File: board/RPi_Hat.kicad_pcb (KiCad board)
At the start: 2 copper layers, 65 x 56.5 mm, 33 parts, among them IC1 ATMEGA328P-P, IC2 RFM69HW, J1 RPi_GPIO, P6 SW_CONN, P7 CONN_01X01, Q1 BSS138_GSD, SW1 SWITCH, Y1 16MHz

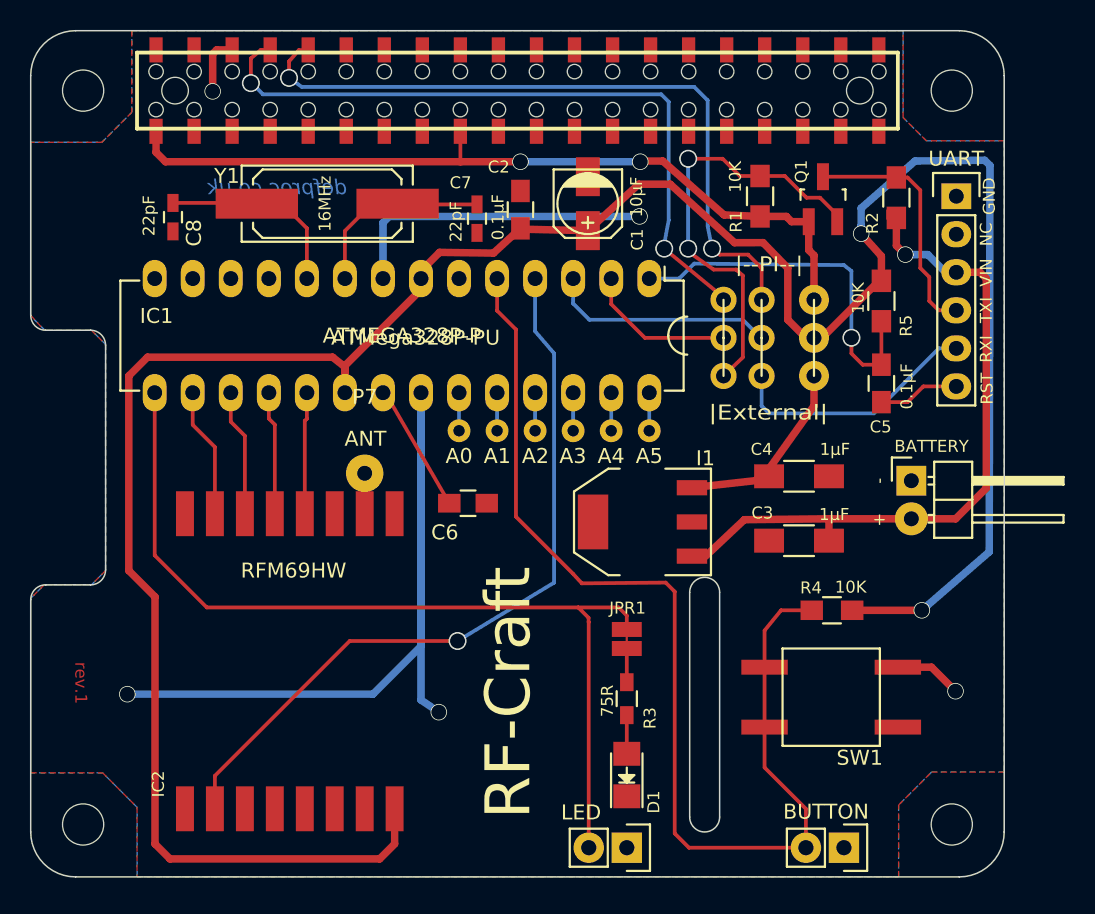
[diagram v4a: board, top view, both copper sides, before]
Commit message: revised via sizes, as per board house recommendations
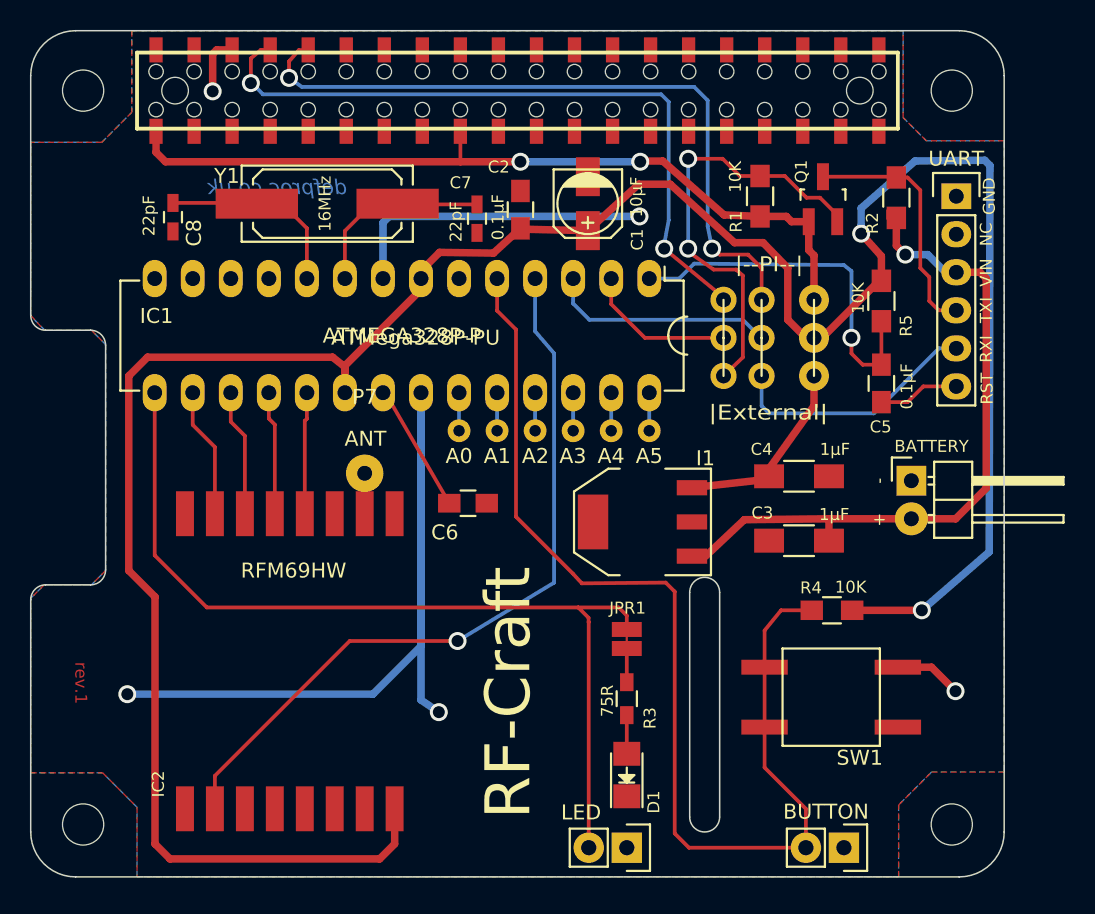
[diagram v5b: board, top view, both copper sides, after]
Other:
- net class BUS: via_dia 1.1 -> 1.2; via_drill 1 -> 0.8
- net class Default: via_drill 1 -> 0.8
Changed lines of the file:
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@@
     (edge_width 0.1)
     (via_size 1.2)
-    (via_drill 1)
+    (via_drill 0.8)
     (via_min_size 0.4)
     (via_min_drill 0.3)
@@
     (trace_width 0.25)
     (via_dia 1.2)
-    (via_drill 1)
+    (via_drill 0.8)
     (uvia_dia 0.6)
     (uvia_drill 0.4)
@@
     (clearance 0.2)
     (trace_width 0.5)
-    (via_dia 1.1)
-    (via_drill 1)
+    (via_dia 1.2)
+    (via_drill 0.8)
     (uvia_dia 0.6)
     (uvia_drill 0.4)
@@
   (gr_line (start 79.2 44.45) (end 138.2 44.45) (angle 90) (layer Edge.Cuts) (width 0.1))
   (segment (start 140.25 53.45) (end 139.9 53.1) (width 0.5) (layer B.Cu) (net 29))
-  (via (at 135.7 83.15) (size 1.1) (drill 1) (layers F.Cu B.Cu) (net 29))
+  (via (at 135.7 83.15) (size 1.2) (drill 0.8) (layers F.Cu B.Cu) (net 29))
   (segment (start 135.7 83.15) (end 140.2 79.25) (width 0.5) (layer B.Cu) (net 29))
   (segment (start 140.2 79.25) (end 140.25 53.45) (width 0.5) (layer B.Cu) (net 29))
@@
   (segment (start 133 59.5) (end 133 61.15) (width 0.5) (layer F.Cu) (net 29))
   (segment (start 131.65 58) (end 133 59.5) (width 0.5) (layer F.Cu) (net 29))
-  (via (at 131.65 58) (size 1.1) (drill 1) (layers F.Cu B.Cu) (net 29))
+  (via (at 131.65 58) (size 1.2) (drill 0.8) (layers F.Cu B.Cu) (net 29))
   (segment (start 131.65 57.45) (end 131.65 58) (width 0.5) (layer B.Cu) (net 29))
   (segment (start 135.25 53.15) (end 131.65 56.3) (width 0.5) (layer B.Cu) (net 29))
@@
   (segment (start 97.18 66.82) (end 97.18 68.62) (width 0.5) (layer F.Cu) (net 29))
   (segment (start 89.65 45.7322) (end 88.6178 45.7322) (width 0.5) (layer F.Cu) (net 30))
-  (via (at 88.35 48.5) (size 1.1) (drill 1) (layers F.Cu B.Cu) (net 30))
+  (via (at 88.35 48.5) (size 1.2) (drill 0.8) (layers F.Cu B.Cu) (net 30))
   (segment (start 88.35 46) (end 88.35 48.5) (width 0.5) (layer F.Cu) (net 30))
   (segment (start 88.6178 45.7322) (end 88.35 46) (width 0.5) (layer F.Cu) (net 30))
   (segment (start 134.1 86.95) (end 136.35 86.95) (width 0.5) (layer F.Cu) (net 30))
-  (via (at 137.95 88.55) (size 1.1) (drill 1) (layers F.Cu B.Cu) (net 30))
+  (via (at 137.95 88.55) (size 1.2) (drill 0.8) (layers F.Cu B.Cu) (net 30))
   (segment (start 136.35 86.95) (end 137.95 88.55) (width 0.5) (layer F.Cu) (net 30))
   (segment (start 99.72 61) (end 99.72 57.27) (width 0.5) (layer B.Cu) (net 30))
-  (via (at 116.85 56.85) (size 1.1) (drill 1) (layers F.Cu B.Cu) (net 30))
+  (via (at 116.85 56.85) (size 1.2) (drill 0.8) (layers F.Cu B.Cu) (net 30))
   (segment (start 100.14 56.85) (end 116.85 56.85) (width 0.5) (layer B.Cu) (net 30))
   (segment (start 99.72 57.27) (end 100.14 56.85) (width 0.5) (layer B.Cu) (net 30))
   (segment (start 102.26 68.62) (end 102.26 85.54) (width 0.5) (layer B.Cu) (net 30))
-  (via (at 82.65 88.75) (size 1.1) (drill 1) (layers F.Cu B.Cu) (net 30))
+  (via (at 82.65 88.75) (size 1.2) (drill 0.8) (layers F.Cu B.Cu) (net 30))
   (segment (start 99.05 88.75) (end 82.65 88.75) (width 0.5) (layer B.Cu) (net 30))
   (segment (start 102.26 85.54) (end 99.05 88.75) (width 0.5) (layer B.Cu) (net 30))
   (segment (start 102.26 68.62) (end 102.26 89.14) (width 0.5) (layer B.Cu) (net 30))
   (segment (start 102.26 89.14) (end 103.45 89.95) (width 0.5) (layer B.Cu) (net 30))
-  (via (at 103.45 89.95) (size 1.1) (drill 1) (layers F.Cu B.Cu) (net 30))
+  (via (at 103.45 89.95) (size 1.2) (drill 0.8) (layers F.Cu B.Cu) (net 30))
   (segment (start 138 60.58) (end 139.58 60.58) (width 0.5) (layer F.Cu) (net 31) (status 10))
   (segment (start 137.96 77.04) (end 135 77.04) (width 0.5) (layer F.Cu) (net 31))
@@
   (segment (start 137.28 60.58) (end 136.1 59.4) (width 0.5) (layer B.Cu) (net 31) (status 10))
   (segment (start 136.1 59.4) (end 134.6 59.4) (width 0.5) (layer B.Cu) (net 31))
-  (via (at 134.6 59.4) (size 1.1) (drill 1) (layers F.Cu B.Cu) (net 31))
+  (via (at 134.6 59.4) (size 1.2) (drill 0.8) (layers F.Cu B.Cu) (net 31))
   (segment (start 134.6 59.4) (end 134 58.8) (width 0.5) (layer F.Cu) (net 31))
   (segment (start 134 58.8) (end 134 56.95) (width 0.5) (layer F.Cu) (net 31))
@@
   (segment (start 117.5 61) (end 119.5 61) (width 0.25) (layer B.Cu) (net 34))
   (segment (start 131 64.95) (end 131 64.95) (width 0.25) (layer F.Cu) (net 34))
-  (via (at 131 64.95) (size 1.2) (drill 1) (layers F.Cu B.Cu) (net 34))
+  (via (at 131 64.95) (size 1.2) (drill 0.8) (layers F.Cu B.Cu) (net 34))
   (segment (start 130.5 60.1) (end 131 60.5) (width 0.25) (layer B.Cu) (net 34))
   (segment (start 131 60.5) (end 131 64.95) (width 0.25) (layer B.Cu) (net 34))
@@
   (segment (start 111.15 81.3) (end 111.15 66) (width 0.25) (layer B.Cu) (net 41))
   (segment (start 104.7 85.2) (end 111.15 81.3) (width 0.25) (layer B.Cu) (net 41))
-  (via (at 104.7 85.2) (size 1.2) (drill 1) (layers F.Cu B.Cu) (net 41))
+  (via (at 104.7 85.2) (size 1.2) (drill 0.8) (layers F.Cu B.Cu) (net 41))
   (segment (start 97.5 85.2) (end 104.7 85.2) (width 0.25) (layer F.Cu) (net 41))
   (segment (start 88.5 94.2) (end 97.5 85.2) (width 0.25) (layer F.Cu) (net 41))
@@
   (segment (start 94.1 45.75) (end 93.45 46.5) (width 0.25) (layer F.Cu) (net 67))
   (segment (start 93.45 46.5) (end 93.45 47.6) (width 0.25) (layer F.Cu) (net 67))
-  (via (at 93.45 47.6) (size 1.2) (drill 1) (layers F.Cu B.Cu) (net 67))
+  (via (at 93.45 47.6) (size 1.2) (drill 0.8) (layers F.Cu B.Cu) (net 67))
   (segment (start 94.73 45.7322) (end 94.1 45.75) (width 0.25) (layer F.Cu) (net 67))
   (segment (start 125 60.3) (end 125 62.42) (width 0.25) (layer F.Cu) (net 67))
@@
   (segment (start 122.2 59.4) (end 124.1 59.4) (width 0.25) (layer F.Cu) (net 67))
   (segment (start 121.7 59) (end 122.2 59.4) (width 0.25) (layer F.Cu) (net 67))
-  (via (at 121.7 59) (size 1.2) (drill 1) (layers F.Cu B.Cu) (net 67))
+  (via (at 121.7 59) (size 1.2) (drill 0.8) (layers F.Cu B.Cu) (net 67))
   (segment (start 121.4 49.1) (end 121.4 57.5) (width 0.25) (layer B.Cu) (net 67))
   (segment (start 121.4 57.5) (end 121.7 59) (width 0.25) (layer B.Cu) (net 67))
@@
   (segment (start 90.9 47.95) (end 91 47.95) (width 0.25) (layer B.Cu) (net 68))
   (segment (start 118.5 59) (end 122.46 62.26) (width 0.25) (layer F.Cu) (net 68))
-  (via (at 118.5 59) (size 1.2) (drill 1) (layers F.Cu B.Cu) (net 68))
+  (via (at 118.5 59) (size 1.2) (drill 0.8) (layers F.Cu B.Cu) (net 68))
   (segment (start 118.45 58.95) (end 118.5 59) (width 0.25) (layer B.Cu) (net 68))
   (segment (start 118.8 49.2) (end 118.8 57.1) (width 0.25) (layer B.Cu) (net 68))
@@
   (segment (start 92.19 45.7322) (end 91.5678 45.7322) (width 0.25) (layer F.Cu) (net 68))
   (segment (start 90.9 47.95) (end 90.8 47.95) (width 0.25) (layer B.Cu) (net 68))
-  (via (at 90.9 47.95) (size 1.2) (drill 1) (layers F.Cu B.Cu) (net 68))
+  (via (at 90.9 47.95) (size 1.2) (drill 0.8) (layers F.Cu B.Cu) (net 68))
   (segment (start 90.9 46.3) (end 90.9 47.95) (width 0.25) (layer F.Cu) (net 68))
   (segment (start 91.5678 45.7322) (end 90.9 46.3) (width 0.25) (layer F.Cu) (net 68))
@@
   (segment (start 118.396014 53.149827) (end 118.4 53.15416) (width 0.25) (layer F.Cu) (net 69))
   (segment (start 116.9 53.2) (end 117 53.3) (width 0.25) (layer F.Cu) (net 69))
-  (via (at 116.9 53.2) (size 1.1) (drill 1) (layers F.Cu B.Cu) (net 69))
+  (via (at 116.9 53.2) (size 1.2) (drill 0.8) (layers F.Cu B.Cu) (net 69))
   (segment (start 108.9 53.2) (end 116.9 53.2) (width 0.5) (layer B.Cu) (net 69))
-  (via (at 108.9 53.2) (size 1.1) (drill 1) (layers F.Cu B.Cu) (net 69))
+  (via (at 108.9 53.2) (size 1.2) (drill 0.8) (layers F.Cu B.Cu) (net 69))
   (segment (start 104.9 53.2) (end 108.9 53.2) (width 0.5) (layer F.Cu) (net 69))
   (segment (start 124.9 56.85) (end 126.65 56.85) (width 0.5) (layer F.Cu) (net 69))
@@
   (segment (start 120.1 58.7) (end 120.1 59.2) (width 0.25) (layer F.Cu) (net 74))
   (segment (start 120.1 59) (end 120.1 58.7) (width 0.25) (layer F.Cu) (net 74))
-  (via (at 120.1 59) (size 1.2) (drill 1) (layers F.Cu B.Cu) (net 74))
+  (via (at 120.1 59) (size 1.2) (drill 0.8) (layers F.Cu B.Cu) (net 74))
   (segment (start 120.1 53) (end 120.1 59) (width 0.25) (layer B.Cu) (net 74))
-  (via (at 120.1 53) (size 1.2) (drill 1) (layers F.Cu B.Cu) (net 74))
+  (via (at 120.1 53) (size 1.2) (drill 0.8) (layers F.Cu B.Cu) (net 74))
   (segment (start 122.4 53) (end 120.1 53) (width 0.25) (layer F.Cu) (net 74))
   (segment (start 123.55 54.15) (end 122.4 53) (width 0.25) (layer F.Cu) (net 74))

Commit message: fixed 3.3v error, and button rotation bug
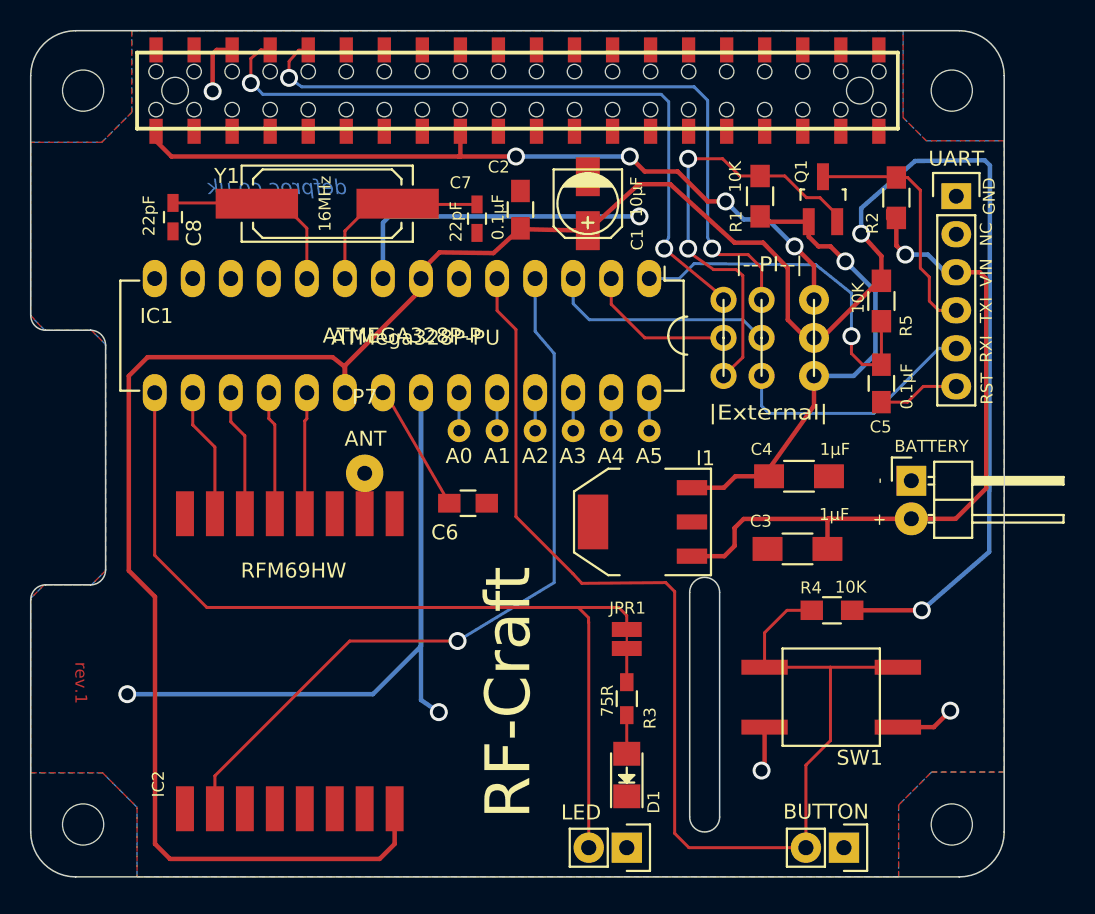
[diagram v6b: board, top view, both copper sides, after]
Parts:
- R3: value 560R -> 75R
- moved C3 0.56 mm to (127.4, 79.0)
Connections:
- P7 pad 1: Net-(IC2-Pad10) -> Net-(P7-Pad1)
- Q1 pad 1: V3.3_PI -> V3.3_BAT
- R1 pad 1: V3.3_PI -> V3.3_BAT
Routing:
- net V3.3_BAT: track 12.9 -> 33.5 mm, vias 0 -> 1
- net SW_D3: track 73.9 -> 82.1 mm
- net V3.3_PI: track 55.1 -> 52.1 mm, vias 2 -> 4
- net Net-(P7-Pad1): track 0.00 -> 2.70 mm
- net Net-(IC2-Pad10): track 2.70 -> 0.00 mm
- net GND: track 89.3 -> 91.7 mm, vias 5 -> 6
- net +BATT: track 46.3 -> 48.6 mm
- net Net-(C5-Pad2): track 24.8 -> 23.8 mm
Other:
- net class BUS: trace_width 0.5 -> 0.3
- net class Default: trace_width 0.25 -> 0.2

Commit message: gerbers and rev1.2 board text
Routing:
- net D2_INT0: track 50.4 -> 54.3 mm
- net D13_SCK: track 8.14 -> 9.14 mm
- net V3.3_BAT: track 33.5 -> 33.0 mm
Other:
- board text added: "Cloudmaker"
- board text added: "rev.1.2"
- board text added: "rev.1.2 2016-05-06"
- board text removed: "rev.1"
- board text removed: "rev.1 2015-10-05"
